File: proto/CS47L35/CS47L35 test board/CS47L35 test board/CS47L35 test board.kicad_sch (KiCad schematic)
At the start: 15 parts, among them U1 CS47L35-CWZR‎, U2 AP2127K-1.8TRG1, U3 MCP1700x-300xxTT

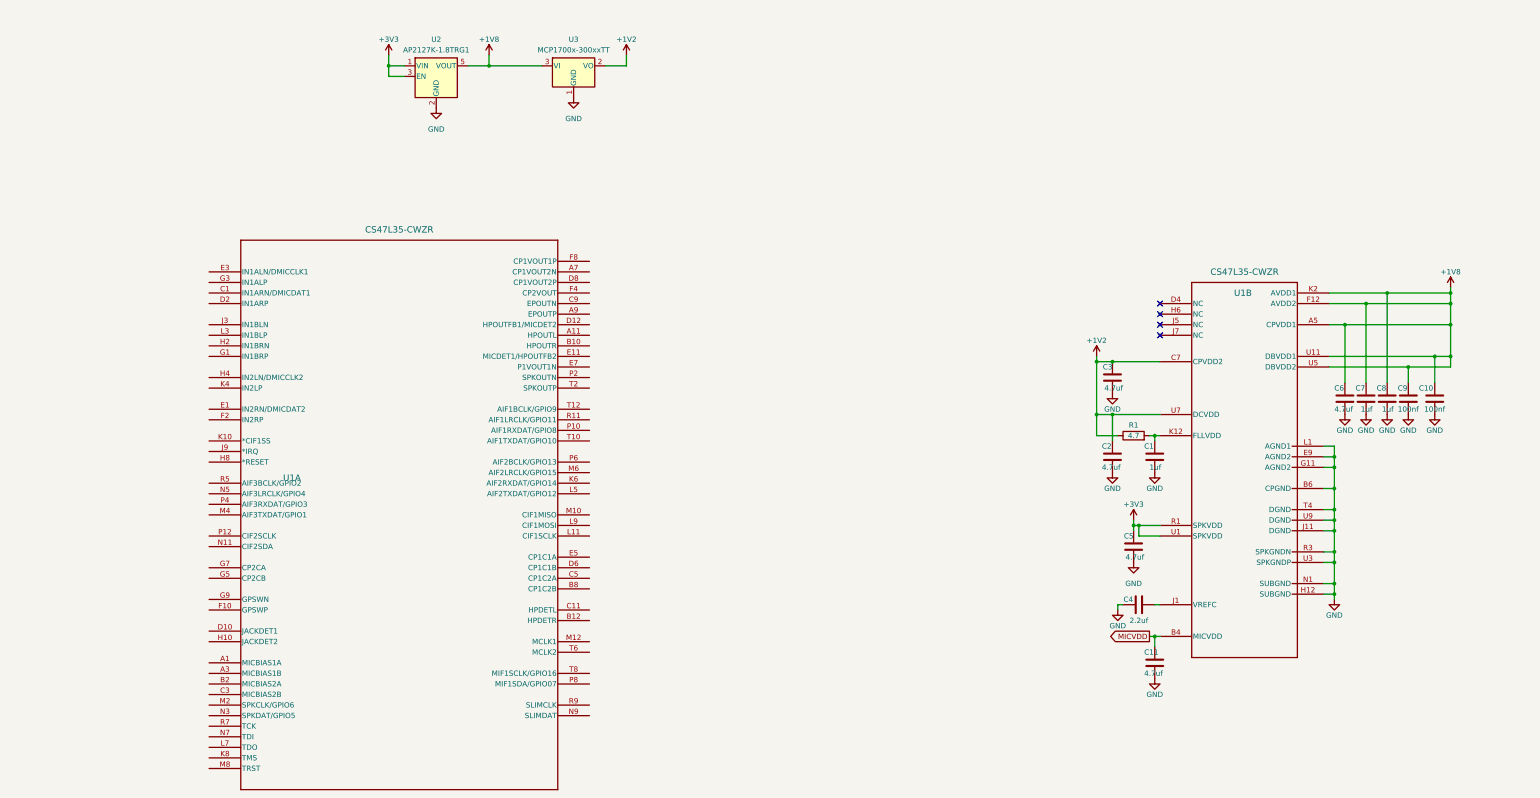
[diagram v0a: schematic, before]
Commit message: cs47l35 rearanged a bit
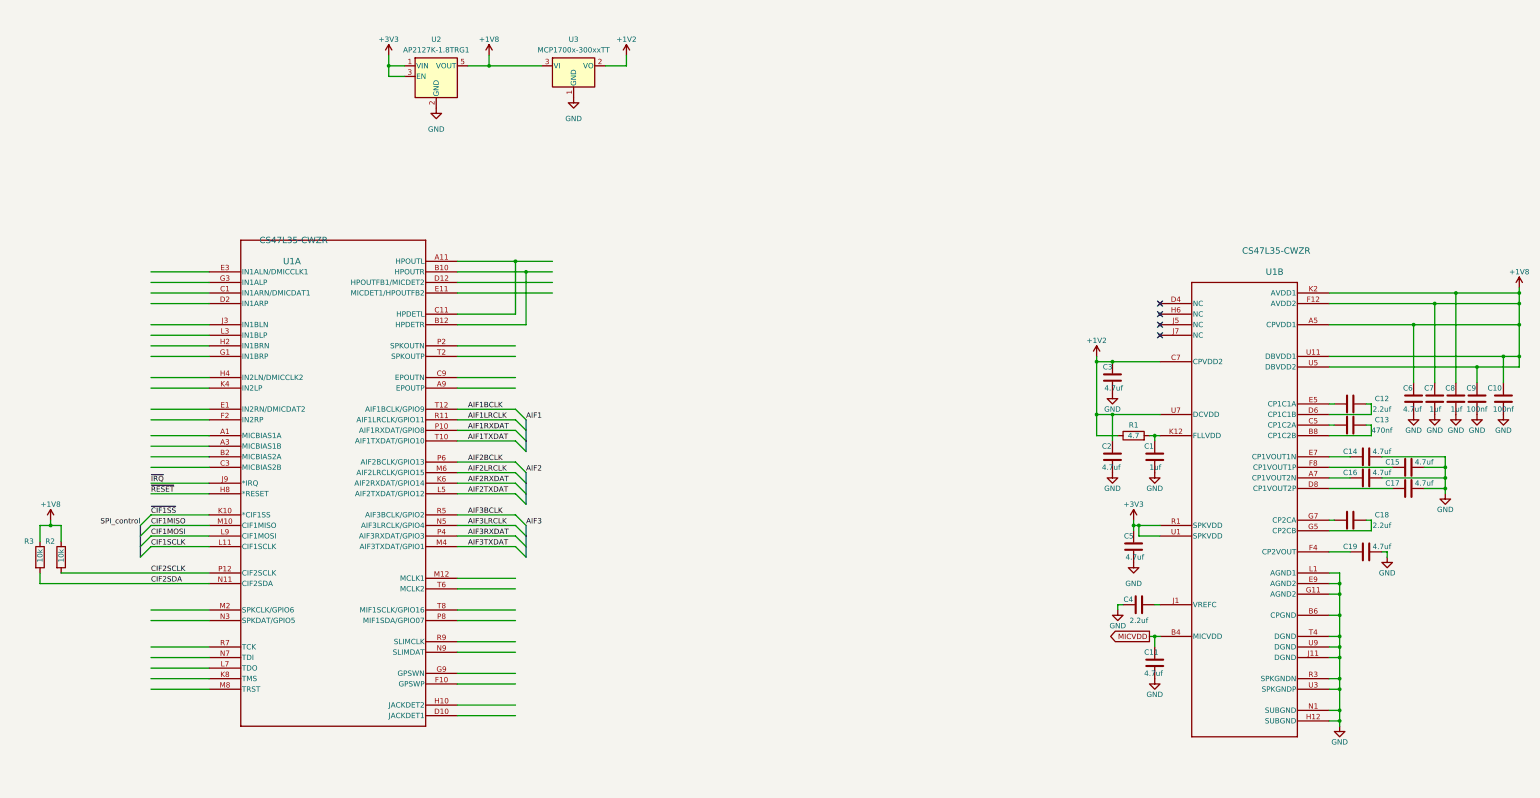
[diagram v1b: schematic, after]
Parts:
- added C12, C18: 2.2uf, Capacitor_SMD:C_0402_1005Metric, symbol !component database:Capacitors/DKGRM155C80J225KE95D
- added C13: 470nf, Capacitor_SMD:C_0402_1005Metric, symbol !component database:Capacitors/DKCL05A474KP5NNNC
- added C14, C15, C16, C17, C19: 4.7uf, Capacitor_SMD:C_0402_1005Metric, symbol !component database:Capacitors/DKCL05A475KQ5NRNC
- added R2, R3: 10k, Resistor_SMD:R_0402_1005Metric, symbol !component database:Resistors/DKPFR05S-103-JNH
- U1: Stock 0 -> 3
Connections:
- net +1V8: now also R2.1, R3.1
- net GND: now also C14.2, C15.2, C16.2, C17.2, C19.2
- net at U1.A11 (HPOUTL): now also U1.C11 (HPDETL)
- net at U1.B10 (HPOUTR): now also U1.B12 (HPDETR)
- net ~{RESET}: now reaches U1.H8 (*RESET)
- net ~{IRQ}: now reaches U1.J9 (*IRQ)
- net ~{CIF1SS}: now reaches U1.K10 (*CIF1SS)
- net AIF2RXDAT: now reaches U1.K6 (AIF2RXDAT/GPIO14)
- net CIF1SCLK: now reaches U1.L11 (CIF1SCLK)
- net AIF2TXDAT: now reaches U1.L5 (AIF2TXDAT/GPIO12)
- net CIF1MOSI: now reaches U1.L9 (CIF1MOSI)
- net CIF1MISO: now reaches U1.M10 (CIF1MISO)
- net AIF3TXDAT: now reaches U1.M4 (AIF3TXDAT/GPIO1)
- net AIF2LRCLK: now reaches U1.M6 (AIF2LRCLK/GPIO15)
- net CIF2SDA: now reaches U1.N11 (CIF2SDA)
- net CIF2SDA: now also R3.2
- net AIF3LRCLK: now reaches U1.N5 (AIF3LRCLK/GPIO4)
- net AIF1RXDAT: now reaches U1.P10 (AIF1RXDAT/GPIO8)
- net CIF2SCLK: now reaches U1.P12 (CIF2SCLK)
- net CIF2SCLK: now also R2.2
- net AIF3RXDAT: now reaches U1.P4 (AIF3RXDAT/GPIO3)
- net AIF2BCLK: now reaches U1.P6 (AIF2BCLK/GPIO13)
- net AIF1LRCLK: now reaches U1.R11 (AIF1LRCLK/GPIO11)
- net AIF3BCLK: now reaches U1.R5 (AIF3BCLK/GPIO2)
- net AIF1TXDAT: now reaches U1.T10 (AIF1TXDAT/GPIO10)
- net AIF1BCLK: now reaches U1.T12 (AIF1BCLK/GPIO9)
- new net: C17.1, U1.D8 (CP1VOUT2P)
- new net: C13.1, U1.C5 (CP1C2A)
- new net: C13.2, U1.B8 (CP1C2B)
- new net: C18.1, U1.G7 (CP2CA)
- new net: C18.2, U1.G5 (CP2CB)
- new net: C12.1, U1.E5 (CP1C1A)
- new net: C12.2, U1.D6 (CP1C1B)
- new net: C14.1, U1.E7 (CP1VOUT1N)
- new net: C19.1, U1.F4 (CP2VOUT)
- new net: C16.1, U1.A7 (CP1VOUT2N)
- new net: C15.1, U1.F8 (CP1VOUT1P)
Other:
- moved on the sheet: C10, C6, C7, C8, C9

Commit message: trying to build on btsdk basic example
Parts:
- removed C1, C7, C8: 1uf, Capacitor_SMD:C_0402_1005Metric, symbol !component database:Capacitors/DKC0402C105K9PAC7867
- removed C10, C9: 100nf, Capacitor_SMD:C_0402_1005Metric, symbol !component database:Capacitors/DKKGM05AR71C104KH
- removed C11, C14, C15, C16, C17, C19, C2, C3, C5, C6: 4.7uf, Capacitor_SMD:C_0402_1005Metric, symbol !component database:Capacitors/DKCL05A475KQ5NRNC
- removed C12, C18, C4: 2.2uf, Capacitor_SMD:C_0402_1005Metric, symbol !component database:Capacitors/DKGRM155C80J225KE95D
- removed C13: 470nf, Capacitor_SMD:C_0402_1005Metric, symbol !component database:Capacitors/DKCL05A474KP5NNNC
- removed R1: 4.7, Resistor_SMD:R_0402_1005Metric, symbol !component database:Resistors/DKRC0402JR-074R7L
- removed R2, R3: 10k, Resistor_SMD:R_0402_1005Metric, symbol !component database:Resistors/DKPFR05S-103-JNH
- removed U1: CS47L35-CWZR‎, Part DB Footprints:BGA_CS47L35-CWZR_CIR, symbol !component database:ICs/DKCS47L35-CWZR‎
- removed U2: AP2127K-1.8TRG1, Package_TO_SOT_SMD:SOT-23-5, symbol !component database:ICs/DKAP2127K-1.8TRG1
- removed U3: MCP1700x-300xxTT, Package_TO_SOT_SMD:SOT-23, symbol !component database:ICs/DKMCP1700T-1202E/TT
- added J1: Conn_01x02, Connector_PinHeader_2.00mm:PinHeader_1x02_P2.00mm_Vertical, symbol Connector_Generic:Conn_01x02
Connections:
- new net I2C_0.CIF2SCLK: J1.1 (Pin_1)
- new net I2C_0.CIF2SDA: J1.2 (Pin_2)
- no-connect marks 4 -> 0
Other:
- added sheet CS47L35 core (CS47L35 core.kicad_sch)
- title: CS47L35 test board -> (none)
